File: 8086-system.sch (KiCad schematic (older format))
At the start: 0 parts

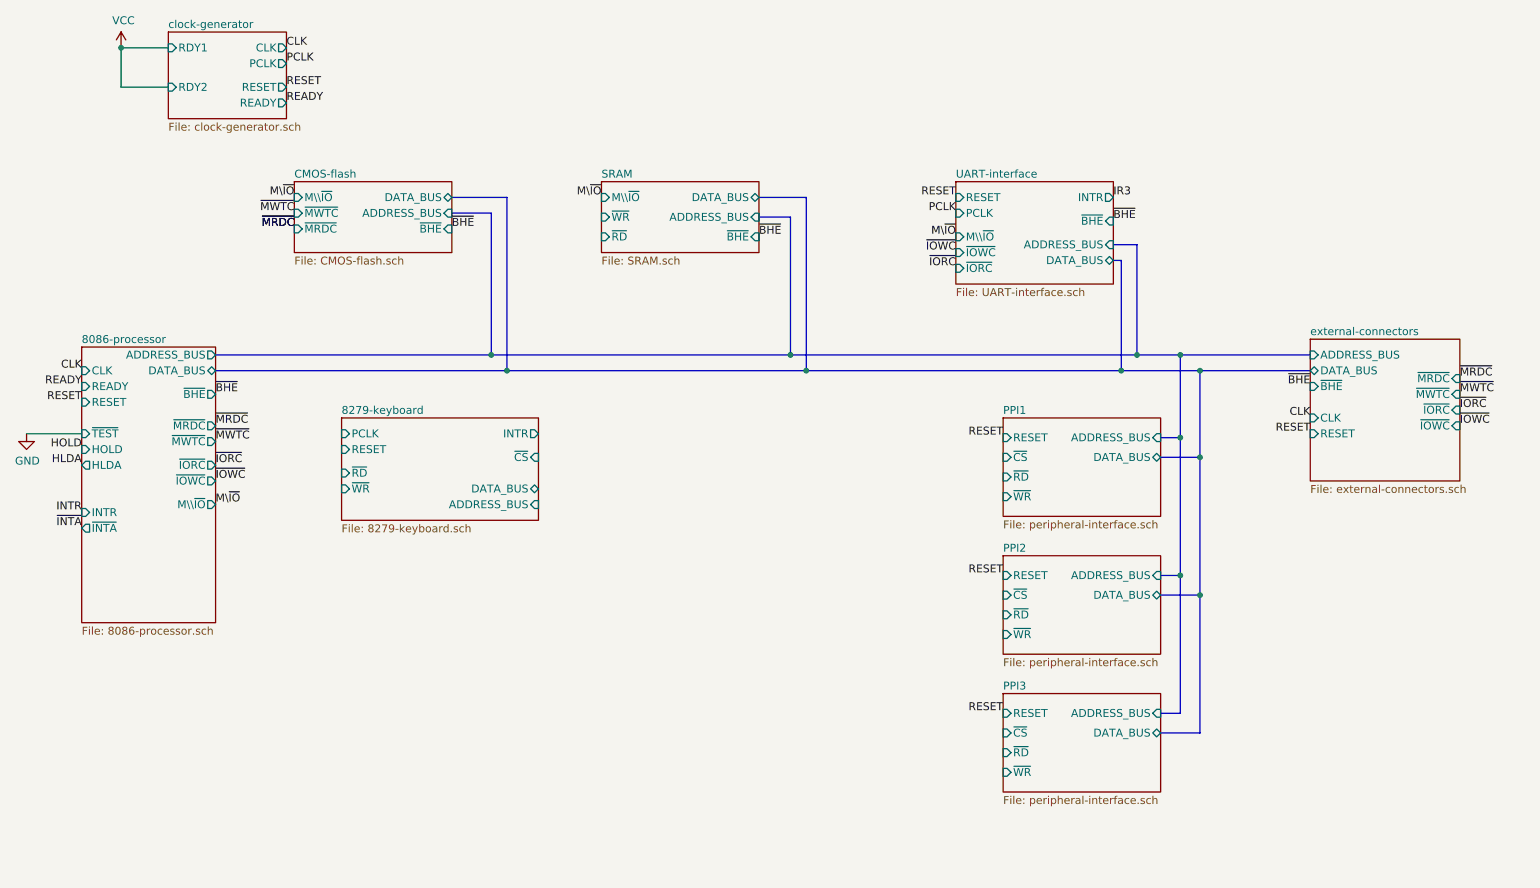
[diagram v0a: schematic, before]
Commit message: Replaced MWTC MRDC IOWC IORC with WR RD; buffered control bus; consolidated logic gates
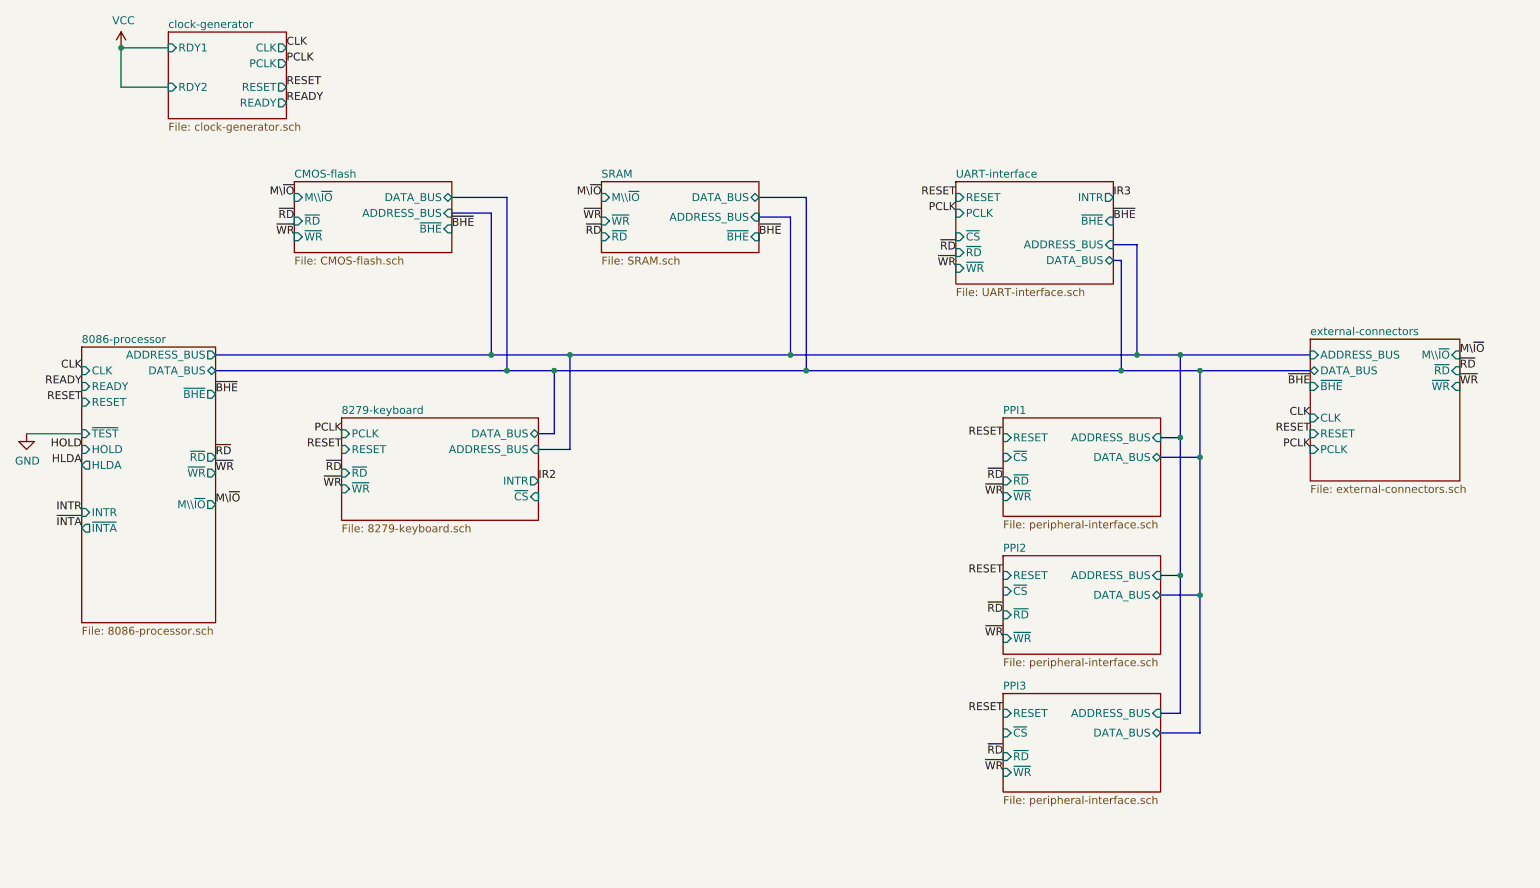
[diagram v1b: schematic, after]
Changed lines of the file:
@@
 $Descr A4 11693 8268
 encoding utf-8
-Sheet 1 10
+Sheet 1 11
 Title "8086-system"
 Date ""
@@
 $EndDescr
 $Sheet
-S 1150 3050 850  1750
-U 6190420C
-F0 "8086-processor" 50
-F1 "8086-processor.sch" 50
-F2 "CLK" I L 1150 3200 50
-F3 "ADDRESS_BUS" O R 2000 3100 50
-F4 "~BHE" O R 2000 3350 50
-F5 "INTR" I L 1150 4100 50
-F6 "RESET" I L 1150 3400 50
-F7 "READY" I L 1150 3300 50
-F8 "~TEST" I L 1150 3600 50
-F9 "HOLD" I L 1150 3700 50
-F10 "HLDA" O L 1150 3800 50
-F11 "~INTA" O L 1150 4200 50
-F12 "~MRDC" O R 2000 3550 50
-F13 "~MWTC" O R 2000 3650 50
-F14 "~IORC" O R 2000 3800 50
-F15 "~IOWC" O R 2000 3900 50
-F16 "DATA_BUS" B R 2000 3200 50
-F17 "M\\~IO" O R 2000 4050 50
-$EndSheet
-$Sheet
 S 8950 3000 950  900
 U 626E3AF4
 F0 "external-connectors" 50
 F1 "external-connectors.sch" 50
-F2 "CLK" I L 8950 3500 50
-F3 "~BHE" I L 8950 3300 50
-F4 "~MRDC" I R 9900 3250 50
-F5 "~MWTC" I R 9900 3350 50
-F6 "~IORC" I R 9900 3450 50
-F7 "~IOWC" I R 9900 3550 50
-F8 "DATA_BUS" B L 8950 3200 50
-F9 "RESET" I L 8950 3600 50
-F10 "ADDRESS_BUS" I L 8950 3100 50
+F2 "~BHE" I L 8950 3300 50
+F3 "DATA_BUS" B L 8950 3200 50
+F4 "ADDRESS_BUS" I L 8950 3100 50
+F5 "CLK" I L 8950 3500 50
+F6 "PCLK" I L 8950 3700 50
+F7 "RESET" I L 8950 3600 50
+F8 "M\\~IO" I R 9900 3100 50
+F9 "~WR" I R 9900 3300 50
+F10 "~RD" I R 9900 3200 50
 $EndSheet
 Text Label 2000 3350 0    50   ~ 0
 ~BHE
-Text Label 2000 3550 0    50   ~ 0
-~MRDC
-Text Label 2000 3650 0    50   ~ 0
-~MWTC
-Text Label 2000 3800 0    50   ~ 0
-~IORC
-Text Label 2000 3900 0    50   ~ 0
-~IOWC
 Text Label 1150 3200 2    50   ~ 0
 CLK
@@
 Text Label 8950 3300 2    50   ~ 0
 ~BHE
-Text Label 9900 3250 0    50   ~ 0
-~MRDC
-Text Label 9900 3350 0    50   ~ 0
-~MWTC
-Text Label 9900 3450 0    50   ~ 0
-~IORC
-Text Label 9900 3550 0    50   ~ 0
-~IOWC
 Wire Bus Line
 	2000 3100 3750 3100
@@
 F0 "CMOS-flash" 50
 F1 "CMOS-flash.sch" 50
-F2 "~MRDC" I L 2500 2300 50
-F3 "DATA_BUS" B R 3500 2100 50
-F4 "ADDRESS_BUS" I R 3500 2200 50
-F5 "M\\~IO" I L 2500 2100 50
-F6 "~BHE" I R 3500 2300 50
-F7 "~MWTC" I L 2500 2200 50
+F2 "DATA_BUS" B R 3500 2100 50
+F3 "ADDRESS_BUS" I R 3500 2200 50
+F4 "M\\~IO" I L 2500 2100 50
+F5 "~BHE" I R 3500 2300 50
+F6 "~WR" I L 2500 2350 50
+F7 "~RD" I L 2500 2250 50
 $EndSheet
 Text Label 3500 2300 0    50   ~ 0
@@
 	3850 2100 3850 3200
 Connection ~ 3850 3200
-Text Label 2500 2300 2    50   ~ 0
-~MRDC
-Text Label 2500 2300 2    50   ~ 0
-~MRDC
-Text Label 2500 2200 2    50   ~ 0
-~MWTC
 Text Label 2500 2100 2    50   ~ 0
 M\~IO
@@
 F1 "UART-interface.sch" 50
 F2 "INTR" O R 7700 2100 50
-F3 "~IORC" I L 6700 2550 50
-F4 "~IOWC" I L 6700 2450 50
-F5 "PCLK" I L 6700 2200 50
-F6 "DATA_BUS" B R 7700 2500 50
-F7 "RESET" I L 6700 2100 50
-F8 "ADDRESS_BUS" I R 7700 2400 50
-F9 "M\\~IO" I L 6700 2350 50
-F10 "~BHE" I R 7700 2250 50
+F3 "PCLK" I L 6700 2200 50
+F4 "DATA_BUS" B R 7700 2500 50
+F5 "RESET" I L 6700 2100 50
+F6 "ADDRESS_BUS" I R 7700 2400 50
+F7 "~BHE" I R 7700 2250 50
+F8 "~RD" I L 6700 2450 50
+F9 "~WR" I L 6700 2550 50
+F10 "~CS" I L 6700 2350 50
 $EndSheet
 Text Label 7700 2250 0    50   ~ 0
@@
 Wire Bus Line
 	7850 2400 7850 3100
-Text Label 6700 2350 2    50   ~ 0
-M\~IO
-Text Label 6700 2450 2    50   ~ 0
-~IOWC
-Text Label 6700 2550 2    50   ~ 0
-~IORC
 Text Label 6700 2200 2    50   ~ 0
 PCLK
@@
 F1 "8279-keyboard.sch" 50
 F2 "PCLK" I L 2800 3600 50
-F3 "INTR" O R 4050 3600 50
+F3 "INTR" O R 4050 3900 50
 F4 "RESET" I L 2800 3700 50
-F5 "DATA_BUS" B R 4050 3950 50
-F6 "ADDRESS_BUS" I R 4050 4050 50
+F5 "DATA_BUS" B R 4050 3600 50
+F6 "ADDRESS_BUS" I R 4050 3700 50
 F7 "~RD" I L 2800 3850 50
 F8 "~WR" I L 2800 3950 50
-F9 "~CS" I R 4050 3750 50
+F9 "~CS" I R 4050 4000 50
 $EndSheet
 Connection ~ 7750 3200
@@
 F4 "~BHE" I R 5450 2350 50
 F5 "~RD" I L 4450 2350 50
-F6 "~WR" I L 4450 2225 50
+F6 "~WR" I L 4450 2250 50
 F7 "DATA_BUS" B R 5450 2100 50
 $EndSheet
@@
 	5750 3200 7750 3200
 Wire Bus Line
-	3750 3100 5650 3100
-Wire Bus Line
-	3850 3200 5750 3200
+	3750 3100 4250 3100
 $Sheet
 S 7000 3500 1000 625
@@
 F2 "RESET" I L 7000 3625 50
 F3 "~CS" I L 7000 3750 50
-F4 "~RD" I L 7000 3875 50
+F4 "~RD" I L 7000 3900 50
 F5 "~WR" I L 7000 4000 50
-F9 "DATA_BUS" B R 8000 3750 50
-F10 "ADDRESS_BUS" I R 8000 3625 50
+F6 "DATA_BUS" B R 8000 3750 50
+F7 "ADDRESS_BUS" I R 8000 3625 50
 $EndSheet
 $Sheet
@@
 F1 "peripheral-interface.sch" 50
 F2 "RESET" I L 7000 4500 50
-F3 "~CS" I L 7000 4625 50
+F3 "~CS" I L 7000 4600 50
 F4 "~RD" I L 7000 4750 50
-F5 "~WR" I L 7000 4875 50
-F9 "DATA_BUS" B R 8000 4625 50
-F10 "ADDRESS_BUS" I R 8000 4500 50
+F5 "~WR" I L 7000 4900 50
+F6 "DATA_BUS" B R 8000 4625 50
+F7 "ADDRESS_BUS" I R 8000 4500 50
 $EndSheet
 $Sheet
@@
 F2 "RESET" I L 7000 5375 50
 F3 "~CS" I L 7000 5500 50
-F4 "~RD" I L 7000 5625 50
+F4 "~RD" I L 7000 5650 50
 F5 "~WR" I L 7000 5750 50
-F9 "DATA_BUS" B R 8000 5500 50
-F10 "ADDRESS_BUS" I R 8000 5375 50
+F6 "DATA_BUS" B R 8000 5500 50
+F7 "ADDRESS_BUS" I R 8000 5375 50
 $EndSheet
 Wire Bus Line
@@
 Wire Bus Line
 	8250 3200 8950 3200
+$Sheet
+S 1150 3050 850  1750
+U 6190420C
+F0 "8086-processor" 50
+F1 "8086-processor.sch" 50
+F2 "CLK" I L 1150 3200 50
+F3 "ADDRESS_BUS" O R 2000 3100 50
+F4 "~BHE" O R 2000 3350 50
+F5 "INTR" I L 1150 4100 50
+F6 "RESET" I L 1150 3400 50
+F7 "READY" I L 1150 3300 50
+F8 "~TEST" I L 1150 3600 50
+F9 "HOLD" I L 1150 3700 50
+F10 "HLDA" O L 1150 3800 50
+F11 "~INTA" O L 1150 4200 50
+F12 "DATA_BUS" B R 2000 3200 50
+F13 "M\\~IO" O R 2000 4050 50
+F14 "~WR" O R 2000 3850 50
+F15 "~RD" O R 2000 3750 50
+$EndSheet
+Text Label 2000 3750 0    50   ~ 0
+~RD
+Text Label 2000 3850 0    50   ~ 0
+~WR
+Text Label 2500 2250 2    50   ~ 0
+~RD
+Text Label 2500 2350 2    50   ~ 0
+~WR
+Text Label 6700 2450 2    50   ~ 0
+~RD
+Text Label 6700 2550 2    50   ~ 0
+~WR
+Text Label 7000 3900 2    50   ~ 0
+~RD
+Text Label 7000 4000 2    50   ~ 0
+~WR
+Text Label 7000 4900 2    50   ~ 0
+~WR
+Text Label 7000 4750 2    50   ~ 0
+~RD
+Text Label 7000 5650 2    50   ~ 0
+~RD
+Text Label 7000 5750 2    50   ~ 0
+~WR
+Text Label 2800 3850 2    50   ~ 0
+~RD
+Text Label 2800 3950 2    50   ~ 0
+~WR
+Text Label 2800 3600 2    50   ~ 0
+PCLK
+Text Label 2800 3700 2    50   ~ 0
+RESET
+Text Label 4450 2350 2    50   ~ 0
+~RD
+Text Label 4450 2250 2    50   ~ 0
+~WR
+Text Label 8950 3700 2    50   ~ 0
+PCLK
+Text Label 9900 3200 0    50   ~ 0
+~RD
+Text Label 9900 3300 0    50   ~ 0
+~WR
+Text Label 9900 3100 0    50   ~ 0
+M\~IO
+Wire Bus Line
+	3850 3200 4150 3200
+Wire Bus Line
+	4050 3600 4150 3600
+Wire Bus Line
+	4150 3600 4150 3200
+Connection ~ 4150 3200
+Wire Bus Line
+	4150 3200 5750 3200
+Wire Bus Line
+	4050 3700 4250 3700
+Wire Bus Line
+	4250 3700 4250 3100
+Connection ~ 4250 3100
+Wire Bus Line
+	4250 3100 5650 3100
+Text Label 4050 3900 0    50   ~ 0
+IR2
 $EndSCHEMATC

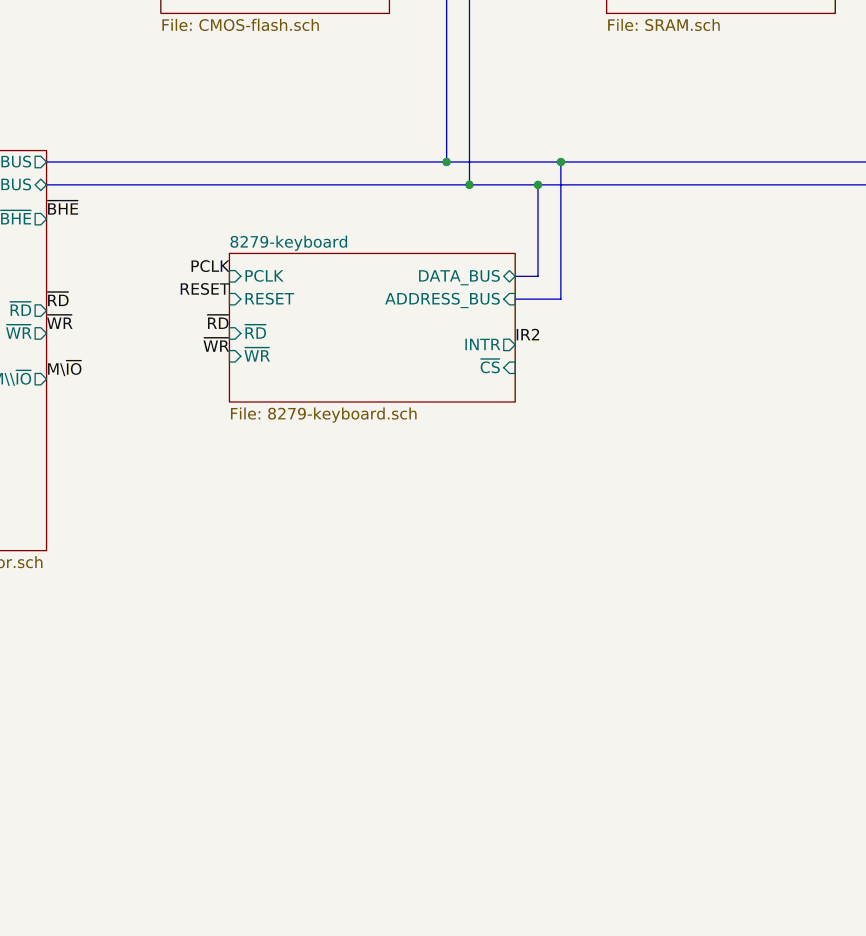
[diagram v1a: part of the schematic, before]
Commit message: created human interface I/O devices
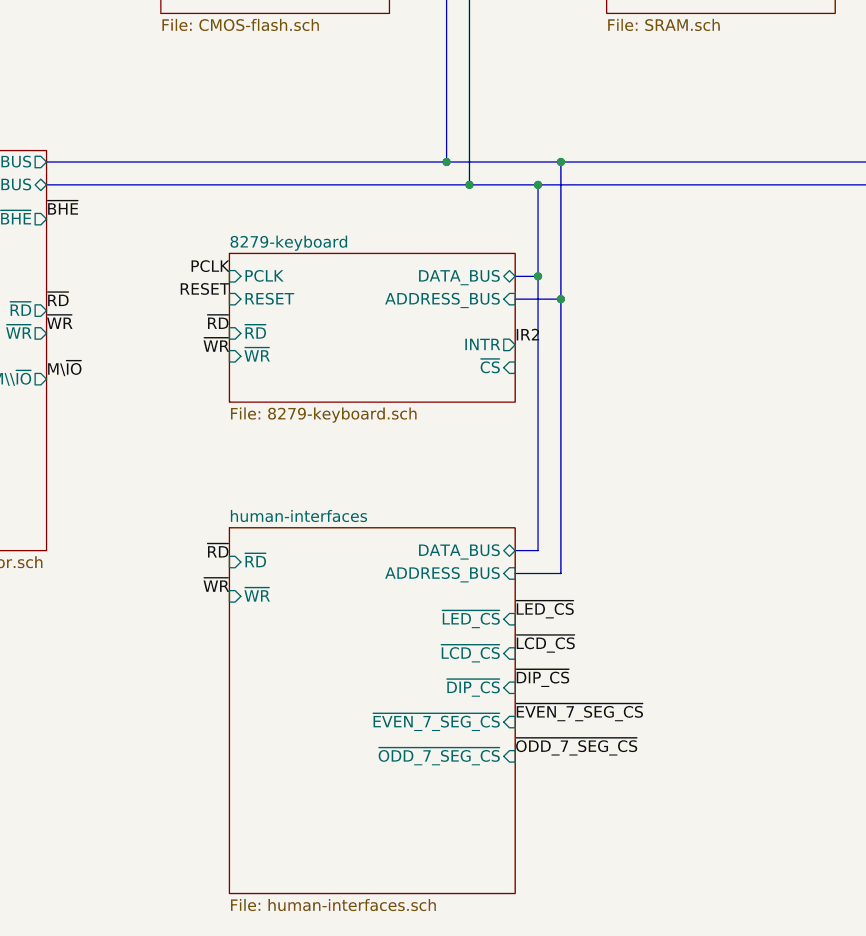
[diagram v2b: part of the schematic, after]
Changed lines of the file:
@@
 $Descr A4 11693 8268
 encoding utf-8
-Sheet 1 11
+Sheet 1 12
 Title "8086-system"
 Date ""
@@
 Wire Bus Line
 	4050 3700 4250 3700
-Wire Bus Line
-	4250 3700 4250 3100
 Connection ~ 4250 3100
 Wire Bus Line
@@
 Text Label 4050 3900 0    50   ~ 0
 IR2
+$Sheet
+S 2800 4700 1250 1600
+U 61CCC9EF
+F0 "human-interfaces" 50
+F1 "human-interfaces.sch" 50
+F2 "DATA_BUS" B R 4050 4800 50
+F3 "ADDRESS_BUS" I R 4050 4900 50
+F4 "~LED_CS" I R 4050 5100 50
+F5 "~LCD_CS" I R 4050 5250 50
+F6 "~DIP_CS" I R 4050 5400 50
+F7 "~EVEN_7_SEG_CS" I R 4050 5550 50
+F8 "~WR" I L 2800 5000 50
+F9 "~ODD_7_SEG_CS" I R 4050 5700 50
+F10 "~RD" I L 2800 4850 50
+$EndSheet
+Text Label 2800 4850 2    50   ~ 0
+~RD
+Text Label 2800 5000 2    50   ~ 0
+~WR
+Wire Bus Line
+	4050 4800 4150 4800
+Wire Bus Line
+	4150 4800 4150 3600
+Connection ~ 4150 3600
+Wire Bus Line
+	4050 4900 4250 4900
+Wire Bus Line
+	4250 3100 4250 3700
+Connection ~ 4250 3700
+Wire Bus Line
+	4250 3700 4250 4900
+Text Label 4050 5100 0    50   ~ 0
+~LED_CS
+Text Label 4050 5250 0    50   ~ 0
+~LCD_CS
+Text Label 4050 5400 0    50   ~ 0
+~DIP_CS
+Text Label 4050 5550 0    50   ~ 0
+~EVEN_7_SEG_CS
+Text Label 4050 5700 0    50   ~ 0
+~ODD_7_SEG_CS
 $EndSCHEMATC
